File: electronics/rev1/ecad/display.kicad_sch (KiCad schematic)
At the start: 51 parts, among them Q1 2N7002, Q10 BSS84, Q11 BSS84, Q13 BSS84, Q2 2N7002, Q3 2N7002, Q4 2N7002, Q5 BSS84, Q6 BSS84, Q7 BSS84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

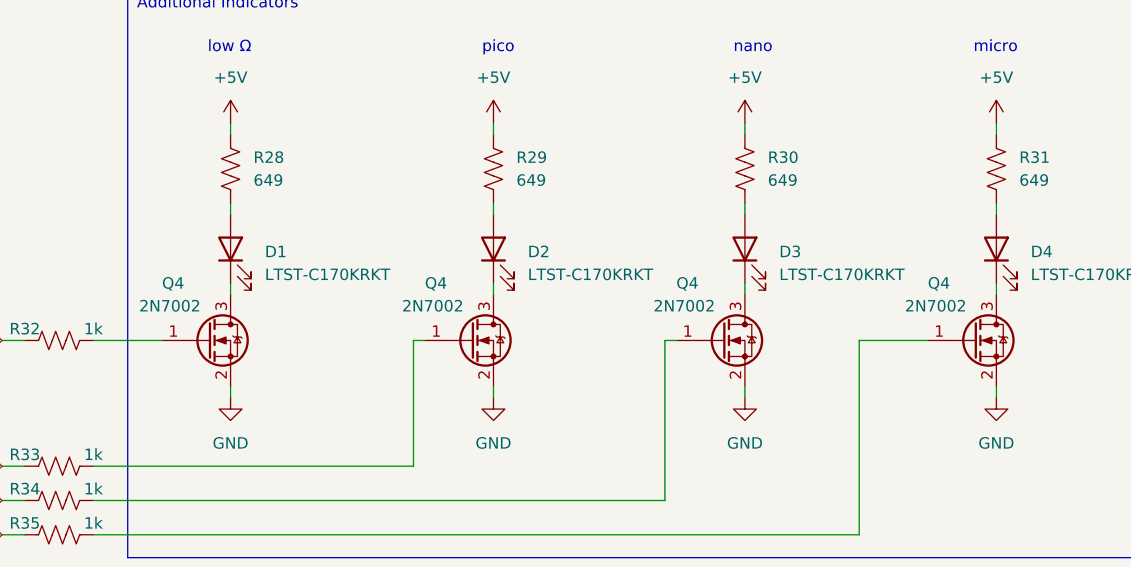
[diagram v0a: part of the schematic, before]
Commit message: proper sign on average voltage
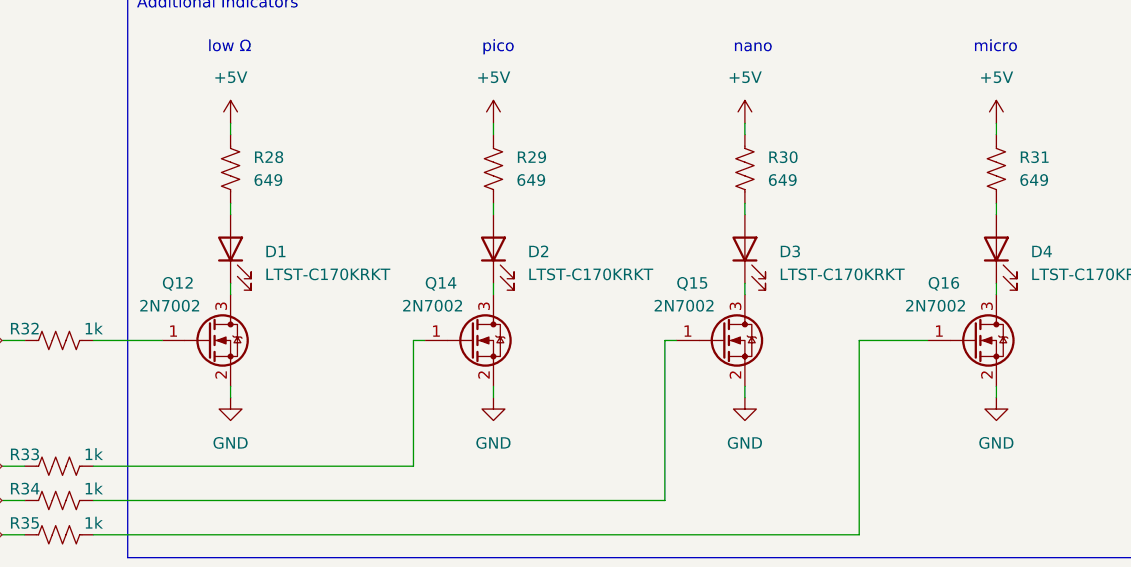
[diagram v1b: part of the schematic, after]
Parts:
- renumbered Q4 to Q12, Q4 to Q14, Q4 to Q15, Q4 to Q16
